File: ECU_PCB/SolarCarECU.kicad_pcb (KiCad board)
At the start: 4 copper layers, 160 x 100 mm, 185 parts, among them J2 Screw_Terminal_01x08, J3 Screw_Terminal_01x08, J4 Screw_Terminal_01x08, J5 Screw_Terminal_01x08, J6 Screw_Terminal_01x08, J7 Screw_Terminal_01x08, J8 Screw_Terminal_01x08, Q1 QM6015D, Q2 QM6015D, Q3 QM6015D, Q4 QM6015D, Q5 QM6015D, Q6 QM6015D, Q7 QM6015D, U1 Teensy3.6, U10 LM324A, U11 MCP1403, U2 MCP1403, U3 MCP1403, U4 L7805, U5 MCP2562-E-P, U6 MCP2562-E-P, U7 4504, U8 4504, U9 4504

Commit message: finished PCB (but forgot to save so commiting again)
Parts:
- G*** (x5): moved to F.Cu
- moved G*** 4.06 mm to (159.3, 68.1), turned to 0 degrees
- moved G*** 3.81 mm to (158.2, 81.5), turned to 0 degrees
- moved G*** 1.78 mm to (179.3, 67.8), turned to 0 degrees
- moved G*** 1.52 mm to (179.3, 80.8), turned to 0 degrees
- turned G*** to 0 degrees

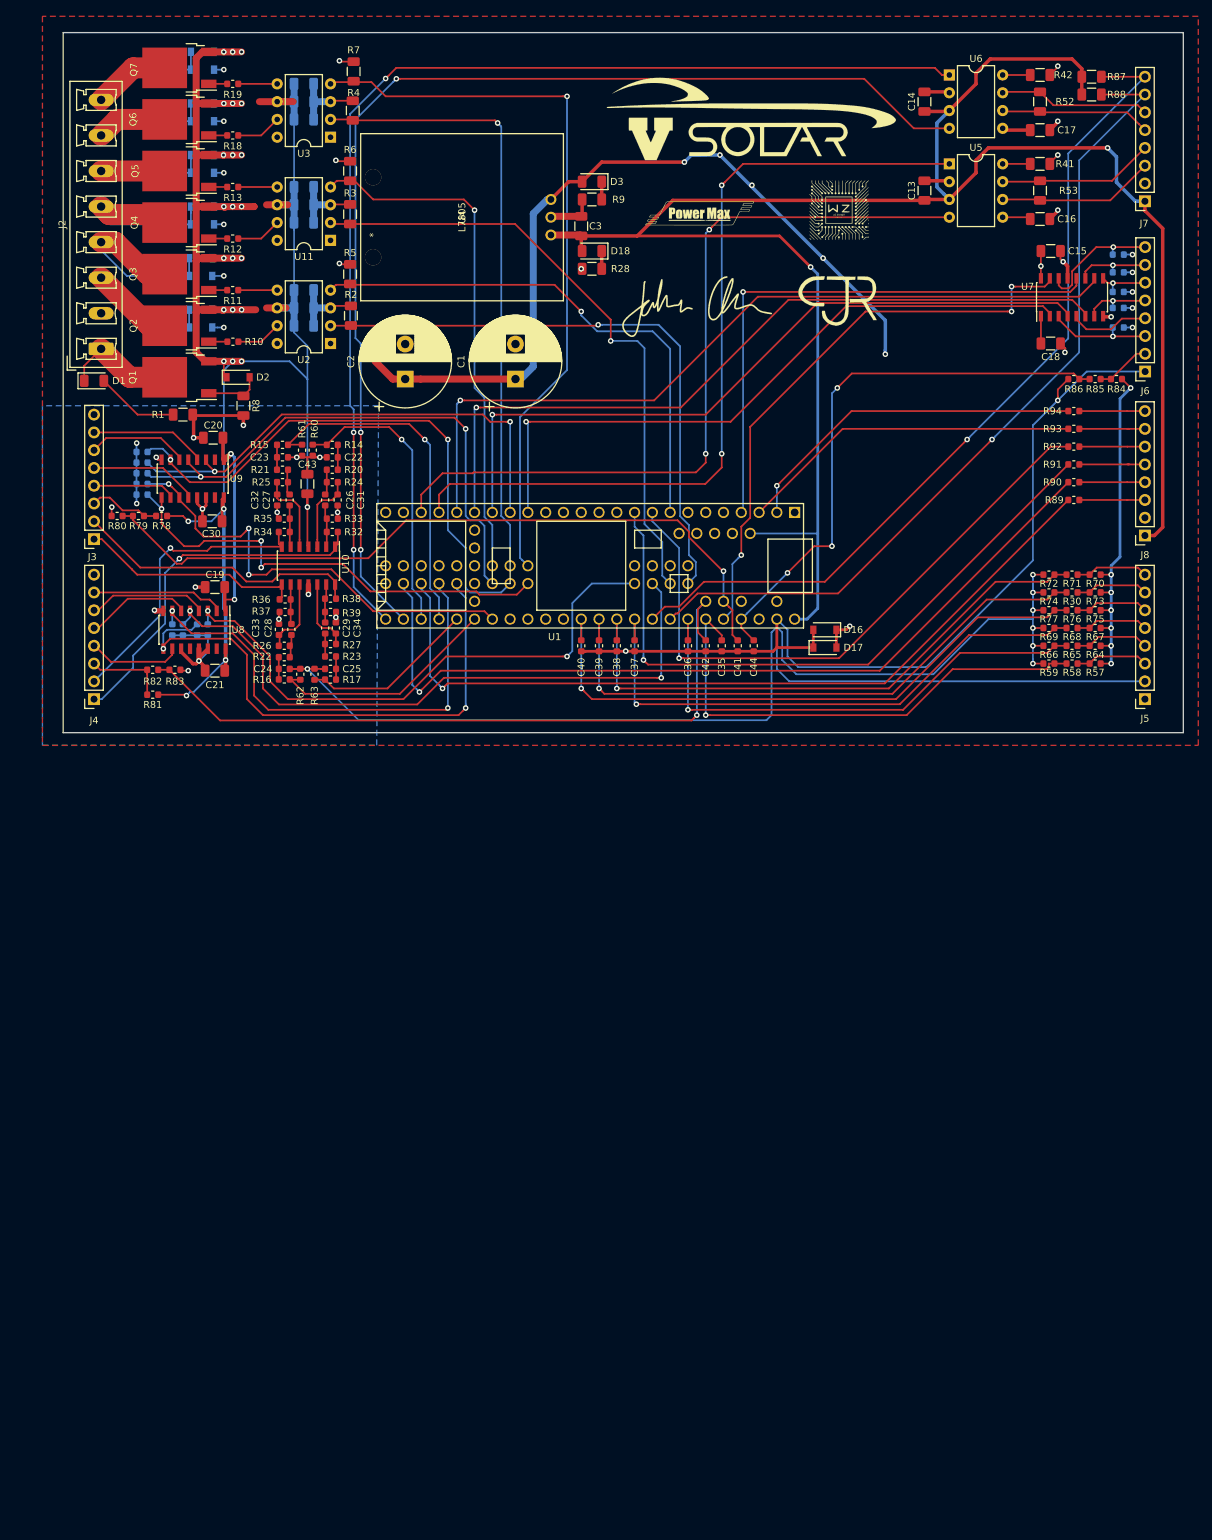
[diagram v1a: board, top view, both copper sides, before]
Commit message: added PTC fuses to all teensy inputs. PCB not modified to match new PCB.
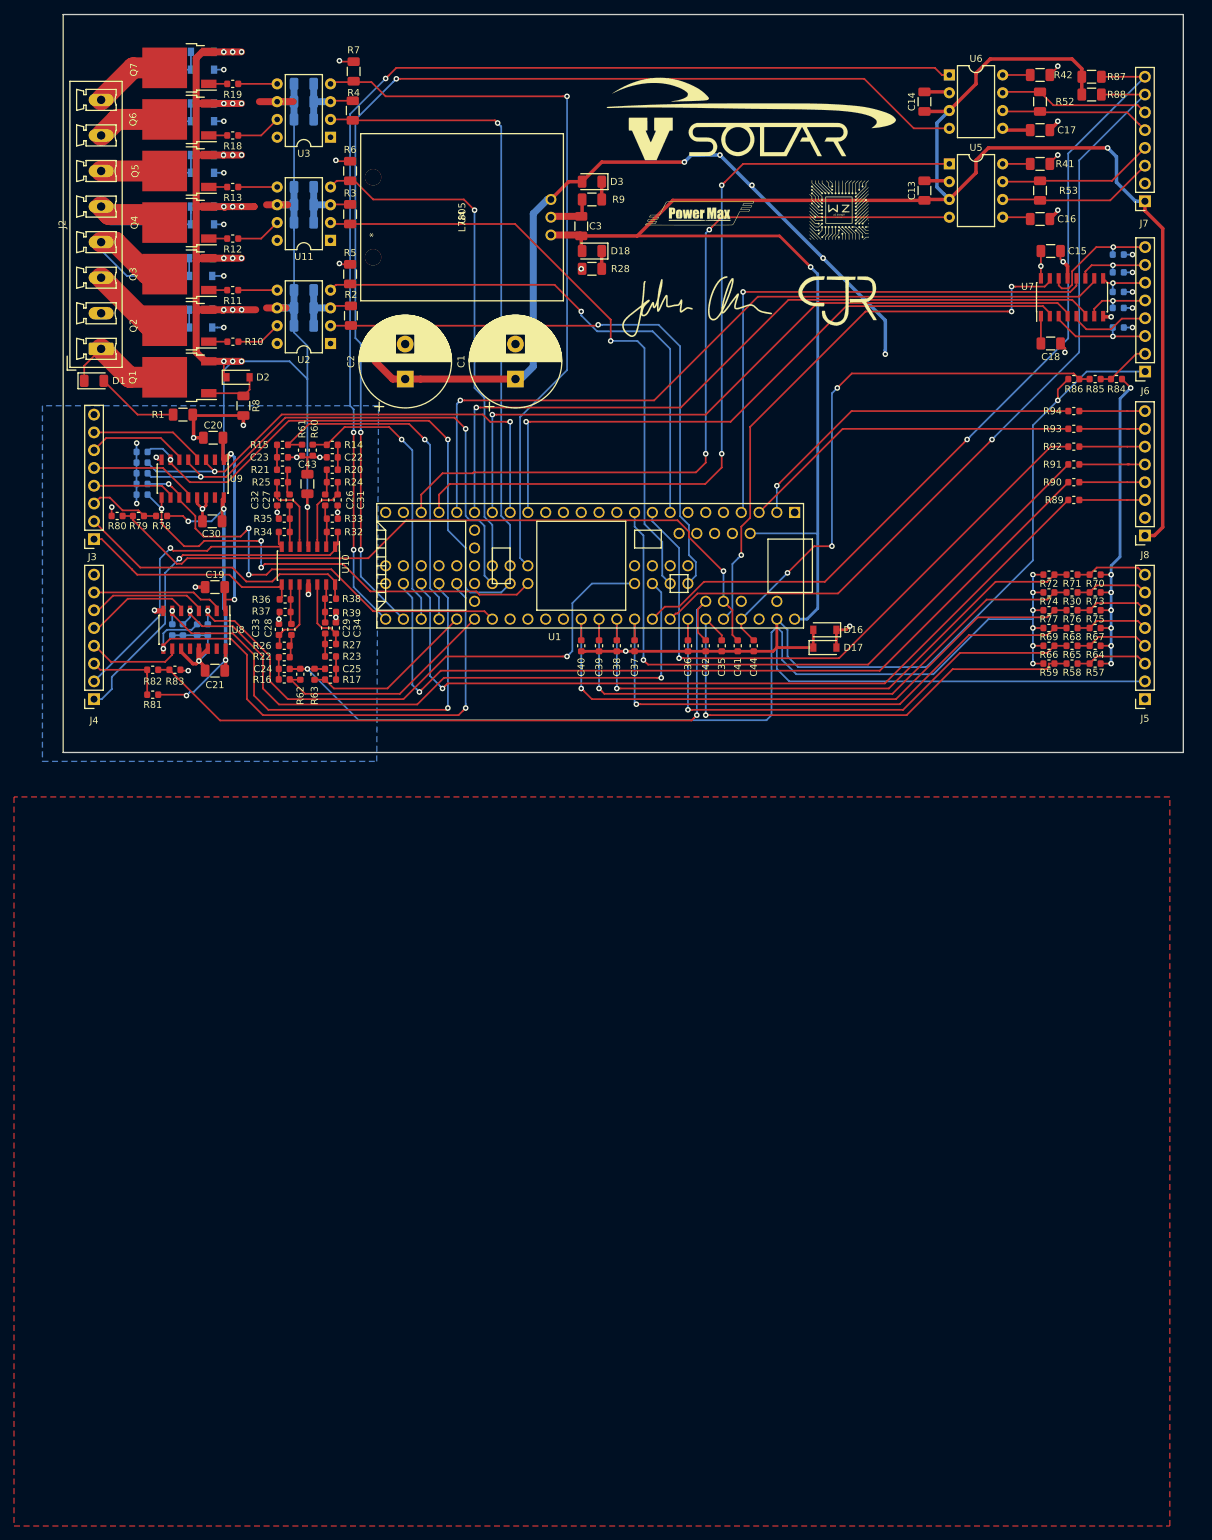
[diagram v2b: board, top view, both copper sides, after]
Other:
- board size 160 x 100 mm -> 160 x 105.4 mm
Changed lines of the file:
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@@
-(kicad_pcb (version 20171130) (host pcbnew 5.1.2-f72e74a~84~ubuntu18.04.1)
+(kicad_pcb (version 20171130) (host pcbnew "(5.1.2)-2")
   (general
     (thickness 1.6)
@@
   (page A4)
   (layers
-    (0 F.Cu signal hide)
+    (0 F.Cu signal)
     (1 In1.Cu power hide)
     (2 In2.Cu power hide)
-    (31 B.Cu signal hide)
+    (31 B.Cu signal)
     (32 B.Adhes user hide)
     (33 F.Adhes user hide)
@@
       (xy 4.956114 -4.263797) (xy 5.029113 -4.270324) (xy 5.078769 -4.264208)) (layer F.SilkS) (width 0.01))
   )
-  (gr_line (start 228.49 142.46) (end 68.49 142.46) (layer Edge.Cuts) (width 0.15))
-  (gr_line (start 68.49 142.46) (end 68.49 42.46) (layer Edge.Cuts) (width 0.15))
+  (gr_line (start 228.49 145.288) (end 68.49 145.288) (layer Edge.Cuts) (width 0.15))
+  (gr_line (start 68.49 145.288) (end 68.49 39.878) (layer Edge.Cuts) (width 0.15))
   (gr_poly (pts (xy 85.09 45.085) (xy 245.11 45.085) (xy 245.11 145.415) (xy 85.09 144.78) (xy 85.09 45.72)) (layer Dwgs.User) (width 0.15))
   (gr_poly (pts (xy 85.09 45.085) (xy 245.11 45.085) (xy 245.11 144.78) (xy 85.09 144.78)) (layer Dwgs.User) (width 0.15))
-  (gr_line (start 228.49 42.46) (end 228.49 142.46) (layer Edge.Cuts) (width 0.15))
-  (gr_line (start 68.49 42.46) (end 228.49 42.46) (layer Edge.Cuts) (width 0.15))
+  (gr_line (start 228.49 39.878) (end 228.49 145.288) (layer Edge.Cuts) (width 0.15))
+  (gr_line (start 68.49 39.878) (end 228.49 39.878) (layer Edge.Cuts) (width 0.15))
   (via (at 166.878 64.262) (size 0.8) (drill 0.4) (layers F.Cu B.Cu) (net 1))
   (segment (start 103.378 115.749018) (end 103.524621 115.895639) (width 0.25) (layer F.Cu) (net 1))
@@
   (segment (start 107.334621 116.345639) (end 106.58626 117.094) (width 0.25) (layer F.Cu) (net 34))
   (segment (start 84.690001 118.001999) (end 85.09 117.602) (width 0.25) (layer B.Cu) (net 34))
+  (segment (start 73.998 137.668) (end 75.438 136.228) (width 0.25) (layer B.Cu) (net 34))
   (segment (start 72.898 137.668) (end 73.998 137.668) (width 0.25) (layer B.Cu) (net 34))
-  (segment (start 78.486 131.443589) (end 83.058 126.871589) (width 0.25) (layer B.Cu) (net 34))
-  (segment (start 73.998 137.668) (end 78.486 133.18) (width 0.25) (layer B.Cu) (net 34))
+  (segment (start 75.438 136.228) (end 75.438 134.491589) (width 0.25) (layer B.Cu) (net 34))
+  (segment (start 75.438 134.491589) (end 83.058 126.871589) (width 0.25) (layer B.Cu) (net 34))
   (segment (start 83.058 126.871589) (end 83.058 119.634) (width 0.25) (layer B.Cu) (net 34))
-  (segment (start 78.486 133.18) (end 78.486 131.443589) (width 0.25) (layer B.Cu) (net 34))
   (segment (start 83.058 119.634) (end 84.690001 118.001999) (width 0.25) (layer B.Cu) (net 34))
   (segment (start 72.898 132.588) (end 73.787 133.477) (width 0.25) (layer F.Cu) (net 35))
@@
     (polygon
       (pts
-        (xy 65.532 40.132) (xy 65.532 144.272) (xy 230.632 144.272) (xy 230.632 40.132)
+        (xy 61.468 151.638) (xy 61.468 255.778) (xy 226.568 255.778) (xy 226.568 151.638)
       )
     )
@@
     (polygon
       (pts
-        (xy 65.532 144.272) (xy 113.284 144.272) (xy 113.538 95.758) (xy 65.532 95.758)
+        (xy 65.532 146.558) (xy 113.284 146.558) (xy 113.538 95.758) (xy 65.532 95.758)
       )
     )
